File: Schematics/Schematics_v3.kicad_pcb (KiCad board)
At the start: 2 copper layers, 77.5 x 96.5 mm, 18 parts, among them U1 TP4056, U2 BH1750, U3 BME688, U4 BU30TD3WG, U5 NRF52840-DONGLE, U6 LIS3DH

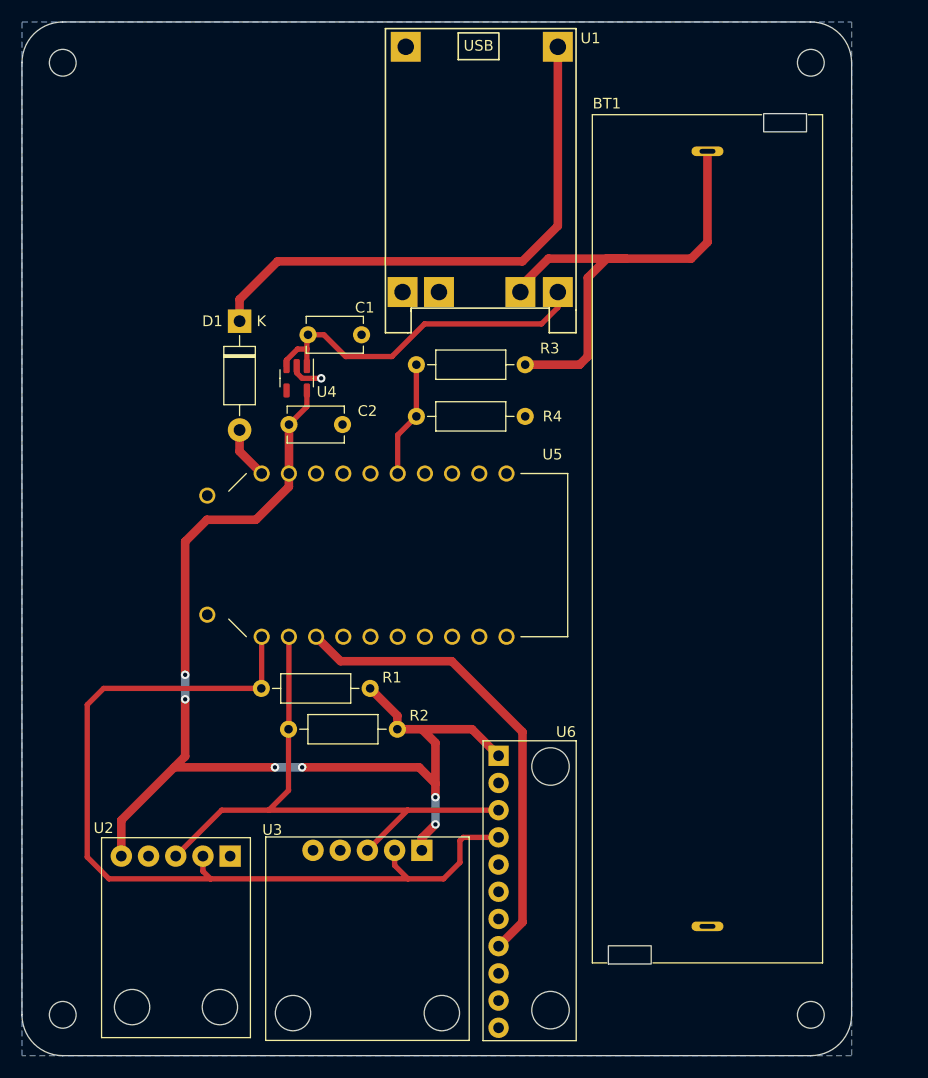
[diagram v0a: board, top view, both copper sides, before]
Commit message: Added a couple prototypes for a pcb
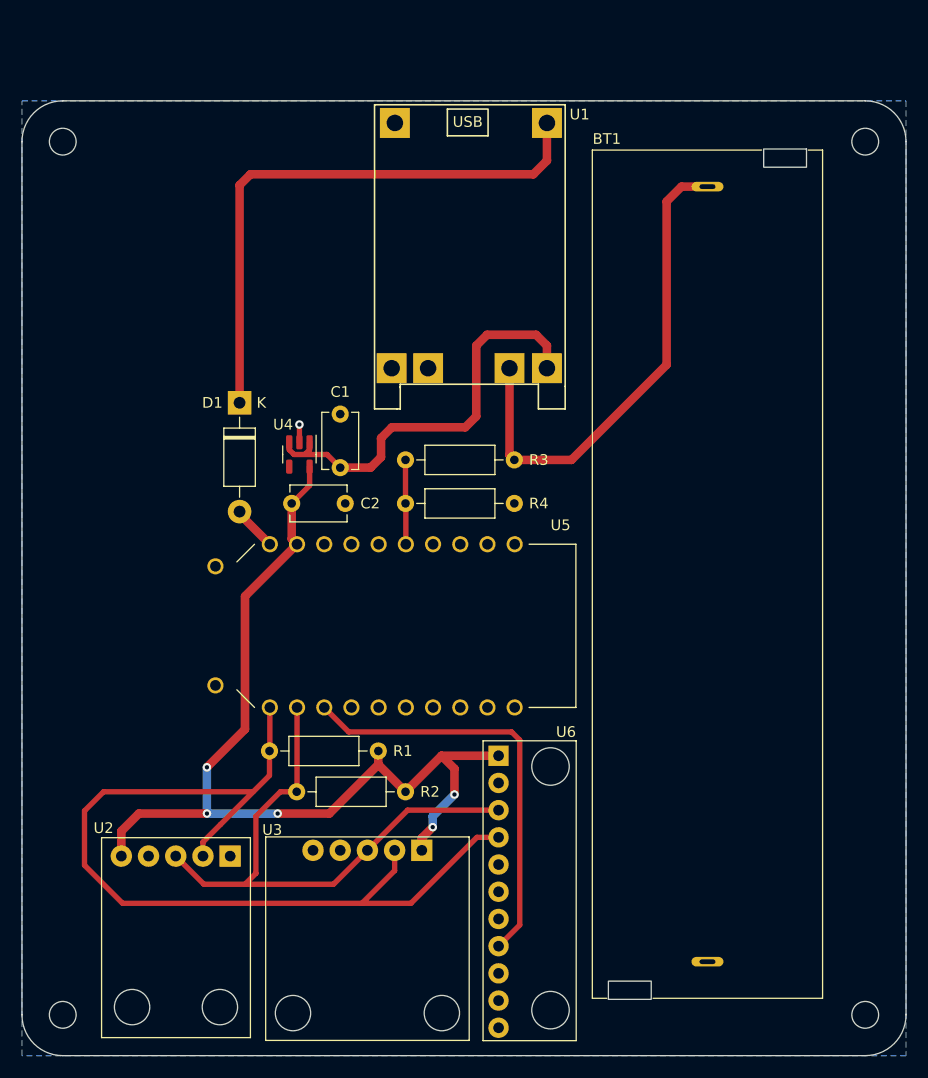
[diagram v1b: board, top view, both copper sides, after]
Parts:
- moved C1 12.8 mm to (113.5, 91.1), turned to 90 degrees
- moved H2 8.95 mm to (162.6, 60.7)
- moved R3 8.95 mm to (129.8, 90.4)
- moved R4 8.19 mm to (129.8, 94.5)
- moved D1 7.62 mm to (104.1, 85.1)
- moved C2 7.37 mm to (109.0, 94.5)
- moved H1 7.37 mm to (87.6, 60.7)
- moved U1 7.18 mm to (134.5, 57.3)
- moved U4 7.12 mm to (109.7, 89.9)
- moved U5 6.65 mm to (112.5, 105.9)
- moved R2 5.89 mm to (109.5, 121.4)
- moved R1 5.89 mm to (117.1, 117.6)
- moved H3 5.08 mm to (162.6, 142.2)
- moved BT1 3.30 mm to (147.8, 101.1)
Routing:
- net +3V0: track 106.0 -> 91.2 mm, vias 6 -> 5
- net VCC: track 33.4 -> 39.3 mm
- net /INT1: track 43.9 -> 39.6 mm
- net /SDA: track 83.6 -> 86.9 mm
- net Net-(R3-Pad2): track 10.9 -> 7.89 mm
- net Net-(D1-Pad1): track 51.3 -> 53.5 mm
- net GND: track 3.13 -> 1.66 mm
- net VBUS: track 4.92 -> 4.22 mm
- net /SCL: track 54.2 -> 53.5 mm
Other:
- board size 77.5 x 96.5 mm -> 82.6 x 89.2 mm
